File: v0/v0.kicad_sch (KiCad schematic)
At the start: 40 parts, among them CON1 SNES-CONN, U1 SN74LV165APWR, U2 SN74LV165APWR, U3 SN74LV165APWR, U4 SN74LVC8T245PWR, U5 PIC12F629-ISN, U6 AMS1117-3.3, U7 SN74LVC8T245PWR, U8 Pico

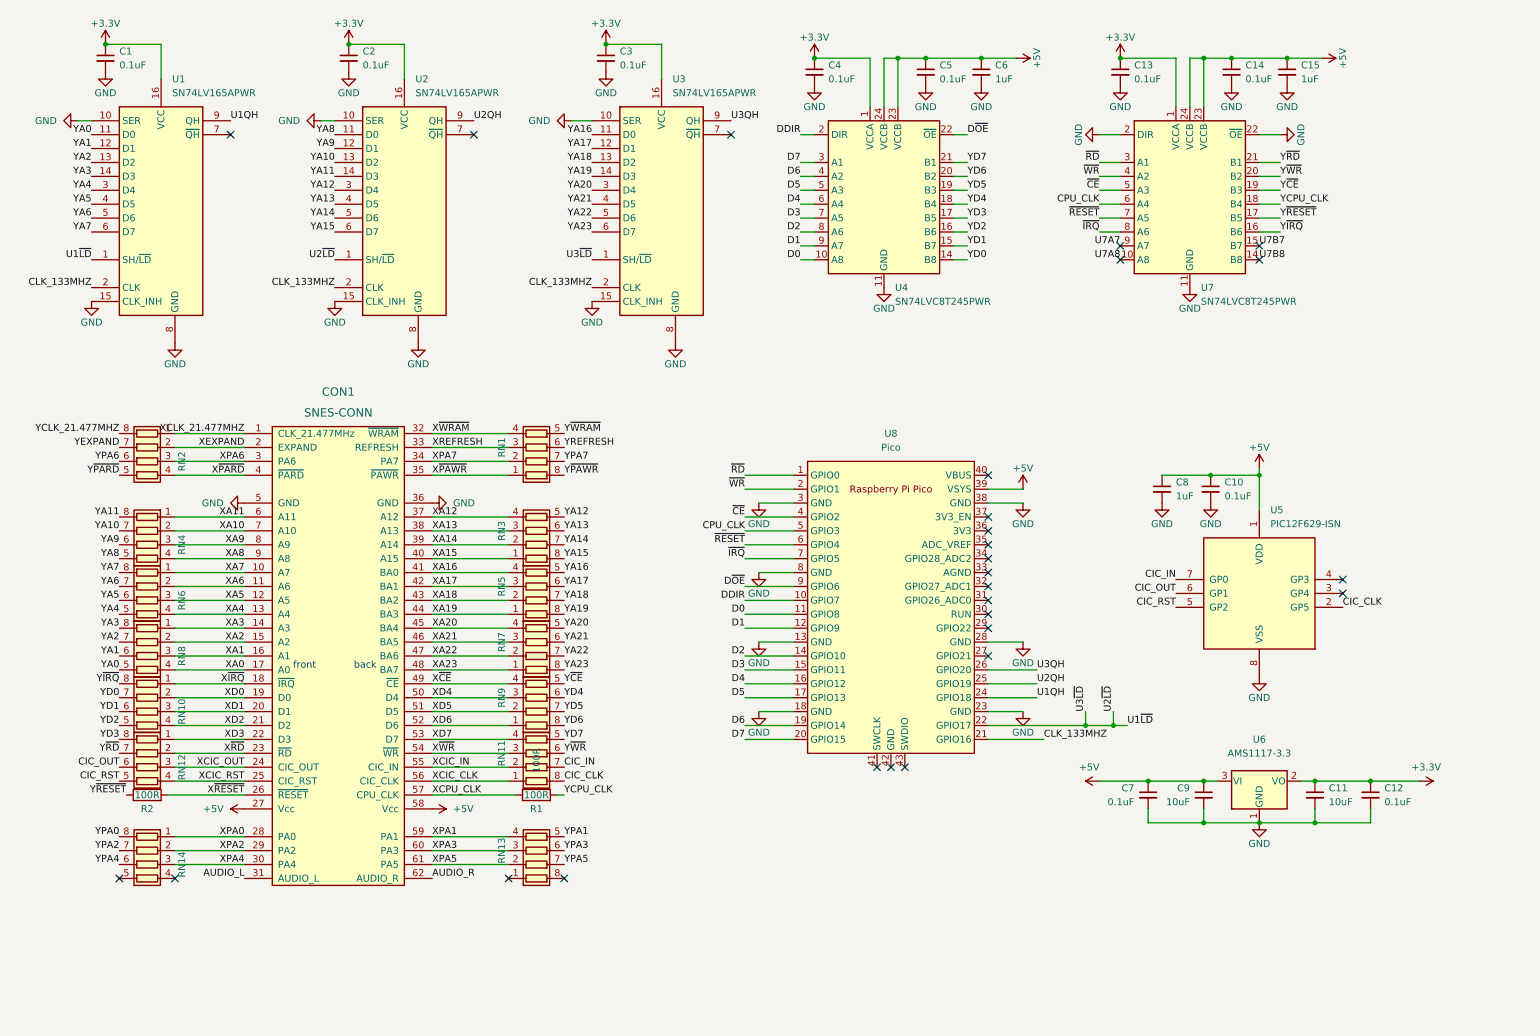
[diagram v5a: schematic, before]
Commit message: Critical fix to PSRAM to control /CE pin from Pico; add LCSC properties to all parts; add ICSP header for PIC12F
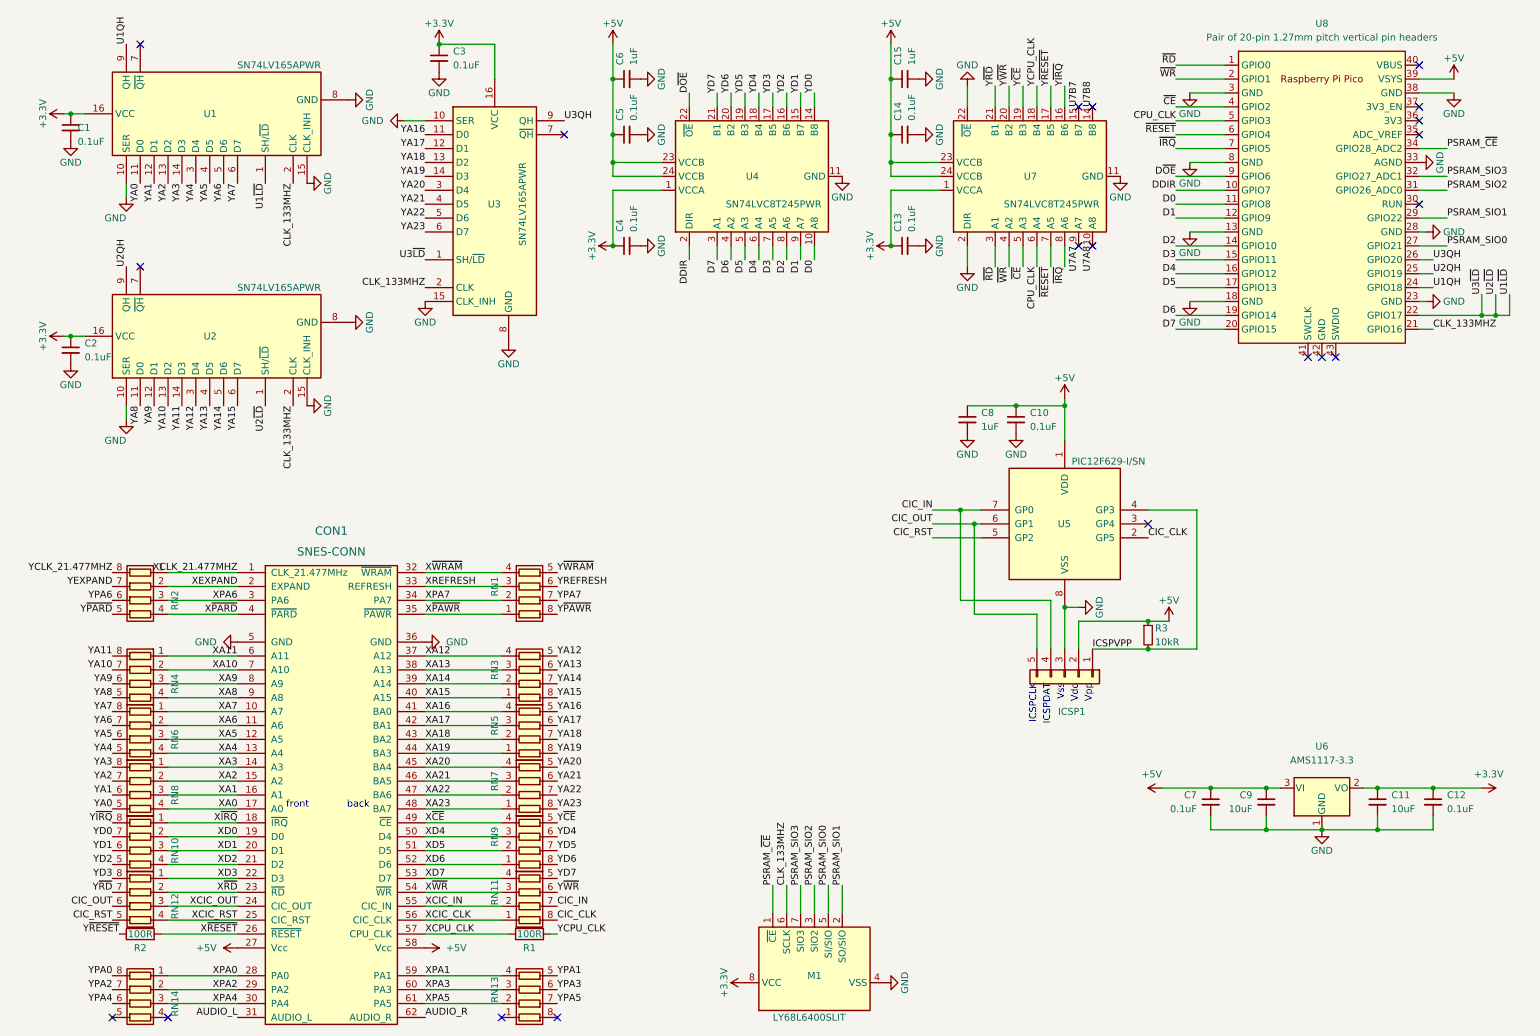
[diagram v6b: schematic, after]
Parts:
- added ICSP1: Conn_01x05, Connector_PinHeader_2.54mm:PinHeader_1x05_P2.54mm_Vertical, symbol Connector_Generic:Conn_01x05
- added M1: LY68L6400SLIT, Package_SO:SOIC-8_3.9x4.9mm_P1.27mm, symbol Memory_RAM:ESP-PSRAM32
- added R3: 10kR, Resistor_SMD:R_1206_3216Metric_Pad1.30x1.75mm_HandSolder, symbol Device:R_Small
- RN1, RN10, RN12, RN13, RN14, RN2, RN3, RN4, RN5, RN6, RN7, RN8: value R_Pack04 -> 100R; LCSC (none) -> C149863
- RN11, RN9: LCSC (none) -> C149863
- U1, U2, U3: LCSC (none) -> C201716
- U4, U7: LCSC (none) -> C27643
- U5: value PIC12F629-ISN -> PIC12F629-I/SN; LCSC (none) -> C8226
- U6: LCSC (none) -> C6186
- U8: value Pico -> Pair of 20-pin 1.27mm pitch vertical pin headers
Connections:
- net +3.3V: now also M1.8 (VCC)
- net +5V: now also ICSP1.2 (Pin_2), R3.1
- net CIC_IN: now also ICSP1.4 (Pin_4)
- net CIC_OUT: now also ICSP1.5 (Pin_5)
- net CLK_133MHZ: now also M1.6 (SCLK)
- net GND: now also U8.33 (AGND), ICSP1.3 (Pin_3), M1.4 (VSS)
- net ICSPVPP: now reaches U5.4 (GP3)
- net ICSPVPP: now also ICSP1.1 (Pin_1), R3.2
- net PSRAM_SIO0: now reaches U8.27 (GPIO21)
- net PSRAM_SIO0: now also M1.5 (SI/SIO)
- net PSRAM_SIO1: now reaches U8.29 (GPIO22)
- net PSRAM_SIO1: now also M1.2 (SO/SIO)
- net PSRAM_SIO2: now reaches U8.31 (GPIO26_ADC0)
- net PSRAM_SIO2: now also M1.3 (SIO2)
- net PSRAM_SIO3: now reaches U8.32 (GPIO27_ADC1)
- net PSRAM_SIO3: now also M1.7 (SIO3)
- net PSRAM_~{CE}: now reaches U8.34 (GPIO28_ADC2)
- net PSRAM_~{CE}: now also M1.1 (~{CE})
- no-connect marks 27 -> 20
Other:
- note added: "ICSPCLK"
- note added: "ICSPDAT"
- note added: "Vdd"
- note added: "Vpp"
- note added: "Vss"
- moved on the sheet: C1, C10, C11, C12, C13, C14, C15, C2, C3, C4, C5, C6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

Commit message: Add JLC properties; re-render front,back,pdf
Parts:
- C1, C10, C11, C12, C13, C14, C15, C2, C3, C4, C5, C6, C7, C8, C9: JLC (none) -> 1206_C
- ICSP1: JLC (none) -> SIP-5_2.5x12.7x2.54P; LCSC (none) -> C492404
- M1: JLC (none) -> SOIC-8
- R1, R2, R3: JLC (none) -> 1206_R
- RN1, RN10, RN11, RN12, RN13, RN14, RN2, RN3, RN4, RN5, RN6, RN7, RN8, RN9: JLC (none) -> RES-ARRAY-SMD
- U1, U2, U3: JLC (none) -> HTSSOP-16_EP_4.4x5.0x0.65P
- U4, U7: JLC (none) -> TSSOP-24_4.4x7.8x0.65P
- U5: JLC (none) -> SOIC-8_3.9x4.9x1.27P
- U6: JLC (none) -> SOT-223
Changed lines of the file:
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@@
+      (effects (font (size 1.27 1.27)) hide)
+    )
+    (property "JLC" "HTSSOP-16_EP_4.4x5.0x0.65P" (id 5) (at 99.06 46.99 0)
       (effects (font (size 1.27 1.27)) hide)
     )
@@
       (effects (font (size 1.27 1.27)) hide)
     )
+    (property "JLC" "HTSSOP-16_EP_4.4x5.0x0.65P" (id 5) (at 46.99 71.12 0)
+      (effects (font (size 1.27 1.27)) hide)
+    )
     (pin "1")
     (pin "10")
@@
     )
     (property "LCSC" "C27643" (id 4) (at 144.78 41.91 90)
+      (effects (font (size 1.27 1.27)) hide)
+    )
+    (property "JLC" "TSSOP-24_4.4x7.8x0.65P" (id 5) (at 144.78 41.91 0)
       (effects (font (size 1.27 1.27)) hide)
     )
@@
       (effects (font (size 1.27 1.27)) hide)
     )
+    (property "JLC" "RES-ARRAY-SMD" (id 5) (at 105.41 172.72 0)
+      (effects (font (size 1.27 1.27)) hide)
+    )
     (pin "1")
     (pin "2")
@@
     )
     (property "LCSC" "C149863" (id 4) (at 105.41 142.24 0)
+      (effects (font (size 1.27 1.27)) hide)
+    )
+    (property "JLC" "RES-ARRAY-SMD" (id 5) (at 105.41 142.24 0)
       (effects (font (size 1.27 1.27)) hide)
     )
@@
       (effects (font (size 1.27 1.27)) hide)
     )
+    (property "JLC" "SOT-223" (id 5) (at 250.19 153.67 0)
+      (effects (font (size 1.27 1.27)) hide)
+    )
     (pin "1")
     (pin "2")
@@
     )
     (property "Datasheet" "~" (id 3) (at 240.03 156.21 0)
+      (effects (font (size 1.27 1.27)) hide)
+    )
+    (property "JLC" "1206_C" (id 4) (at 240.03 156.21 0)
       (effects (font (size 1.27 1.27)) hide)
     )
@@
       (effects (font (size 1.27 1.27)) hide)
     )
+    (property "JLC" "RES-ARRAY-SMD" (id 5) (at 105.41 190.5 0)
+      (effects (font (size 1.27 1.27)) hide)
+    )
     (pin "1")
     (pin "2")
@@
       (effects (font (size 1.27 1.27)) hide)
     )
+    (property "JLC" "RES-ARRAY-SMD" (id 5) (at 34.29 144.78 0)
+      (effects (font (size 1.27 1.27)) hide)
+    )
     (pin "1")
     (pin "2")
@@
     )
     (property "Datasheet" "~" (id 3) (at 123.19 34.29 0)
+      (effects (font (size 1.27 1.27)) hide)
+    )
+    (property "JLC" "1206_C" (id 4) (at 123.19 34.29 0)
       (effects (font (size 1.27 1.27)) hide)
     )
@@
       (effects (font (size 1.27 1.27)) hide)
     )
+    (property "JLC" "1206_R" (id 4) (at 105.41 180.34 0)
+      (effects (font (size 1.27 1.27)) hide)
+    )
     (pin "1")
     (pin "2")
@@
     )
     (property "Datasheet" "~" (id 3) (at 270.51 156.21 0)
+      (effects (font (size 1.27 1.27)) hide)
+    )
+    (property "JLC" "1206_C" (id 4) (at 270.51 156.21 0)
       (effects (font (size 1.27 1.27)) hide)
     )
@@
       (effects (font (size 1.27 1.27)) hide)
     )
+    (property "JLC" "RES-ARRAY-SMD" (id 5) (at 34.29 154.94 0)
+      (effects (font (size 1.27 1.27)) hide)
+    )
     (pin "1")
     (pin "2")
@@
     )
     (property "LCSC" "C27643" (id 4) (at 195.58 41.91 90)
+      (effects (font (size 1.27 1.27)) hide)
+    )
+    (property "JLC" "TSSOP-24_4.4x7.8x0.65P" (id 5) (at 195.58 41.91 0)
       (effects (font (size 1.27 1.27)) hide)
     )
@@
       (effects (font (size 1.27 1.27)) hide)
     )
+    (property "JLC" "RES-ARRAY-SMD" (id 5) (at 34.29 119.38 0)
+      (effects (font (size 1.27 1.27)) hide)
+    )
     (pin "1")
     (pin "2")
@@
     )
     (property "Datasheet" "~" (id 3) (at 260.35 156.21 0)
+      (effects (font (size 1.27 1.27)) hide)
+    )
+    (property "JLC" "1206_C" (id 4) (at 260.35 156.21 0)
       (effects (font (size 1.27 1.27)) hide)
     )
@@
       (effects (font (size 1.27 1.27)) hide)
     )
+    (property "JLC" "RES-ARRAY-SMD" (id 5) (at 34.29 175.26 0)
+      (effects (font (size 1.27 1.27)) hide)
+    )
     (pin "1")
     (pin "2")
@@
       (effects (font (size 1.27 1.27)) hide)
     )
+    (property "JLC" "RES-ARRAY-SMD" (id 5) (at 34.29 134.62 0)
+      (effects (font (size 1.27 1.27)) hide)
+    )
     (pin "1")
     (pin "2")
@@
     )
     (property "LCSC" "C201716" (id 4) (at 46.99 30.48 0)
+      (effects (font (size 1.27 1.27)) hide)
+    )
+    (property "JLC" "HTSSOP-16_EP_4.4x5.0x0.65P" (id 5) (at 46.99 30.48 0)
       (effects (font (size 1.27 1.27)) hide)
     )
@@
       (effects (font (size 1.27 1.27)) hide)
     )
+    (property "JLC" "1206_C" (id 4) (at 185.42 86.36 0)
+      (effects (font (size 1.27 1.27)) hide)
+    )
     (pin "1")
     (pin "2")
@@
       (effects (font (size 1.27 1.27)) hide)
     )
+    (property "JLC" "1206_C" (id 4) (at 194.31 86.36 0)
+      (effects (font (size 1.27 1.27)) hide)
+    )
     (pin "1")
     (pin "2")
@@
       (effects (font (size 1.27 1.27)) hide)
     )
+    (property "JLC" "1206_C" (id 4) (at 21.59 73.66 0)
+      (effects (font (size 1.27 1.27)) hide)
+    )
     (pin "1")
     (pin "2")
@@
       (effects (font (size 1.27 1.27)) hide)
     )
+    (property "JLC" "RES-ARRAY-SMD" (id 5) (at 34.29 193.04 0)
+      (effects (font (size 1.27 1.27)) hide)
+    )
     (pin "1")
     (pin "2")
@@
       (effects (font (size 1.27 1.27)) hide)
     )
+    (property "JLC" "1206_C" (id 4) (at 88.9 20.32 0)
+      (effects (font (size 1.27 1.27)) hide)
+    )
     (pin "1")
     (pin "2")
@@
     )
     (property "Datasheet" "~" (id 3) (at 123.19 54.61 0)
+      (effects (font (size 1.27 1.27)) hide)
+    )
+    (property "JLC" "1206_C" (id 4) (at 123.19 54.61 0)
       (effects (font (size 1.27 1.27)) hide)
     )
@@
       (effects (font (size 1.27 1.27)) hide)
     )
+    (property "JLC" "RES-ARRAY-SMD" (id 5) (at 105.41 152.4 0)
+      (effects (font (size 1.27 1.27)) hide)
+    )
     (pin "1")
     (pin "2")
@@
     )
     (property "Datasheet" "~" (id 3) (at 229.87 156.21 0)
+      (effects (font (size 1.27 1.27)) hide)
+    )
+    (property "JLC" "1206_C" (id 4) (at 229.87 156.21 0)
       (effects (font (size 1.27 1.27)) hide)
     )
@@
       (effects (font (size 1.27 1.27)) hide)
     )
+    (property "JLC" "SOIC-8_3.9x4.9x1.27P" (id 5) (at 203.2 105.41 0)
+      (effects (font (size 1.27 1.27)) hide)
+    )
     (pin "1")
     (pin "2")
@@
       (effects (font (size 1.27 1.27)) hide)
     )
+    (property "JLC" "RES-ARRAY-SMD" (id 5) (at 105.41 132.08 0)
+      (effects (font (size 1.27 1.27)) hide)
+    )
     (pin "1")
     (pin "2")
@@
     )
     (property "Datasheet" "~" (id 3) (at 173.99 54.61 0)
+      (effects (font (size 1.27 1.27)) hide)
+    )
+    (property "JLC" "1206_C" (id 4) (at 173.99 54.61 0)
       (effects (font (size 1.27 1.27)) hide)
     )
@@
       (effects (font (size 1.27 1.27)) hide)
     )
+    (property "JLC" "SOIC-8" (id 5) (at 157.48 186.69 0)
+      (effects (font (size 1.27 1.27)) hide)
+    )
     (pin "1")
     (pin "2")
@@
     )
     (property "Datasheet" "~" (id 3) (at 21.59 33.02 0)
+      (effects (font (size 1.27 1.27)) hide)
+    )
+    (property "JLC" "1206_C" (id 4) (at 21.59 33.02 0)
       (effects (font (size 1.27 1.27)) hide)
     )
@@
       (effects (font (size 1.27 1.27)) hide)
     )
+    (property "LCSC" "C492404" (id 4) (at 203.2 133.35 90)
+      (effects (font (size 1.27 1.27)) hide)
+    )
+    (property "JLC" "SIP-5_2.5x12.7x2.54P" (id 5) (at 203.2 133.35 90)
+      (effects (font (size 1.27 1.27)) hide)
+    )
     (pin "1")
     (pin "2")
@@
     )
     (property "LCSC" "C149863" (id 4) (at 34.29 165.1 0)
+      (effects (font (size 1.27 1.27)) hide)
+    )
+    (property "JLC" "RES-ARRAY-SMD" (id 5) (at 34.29 165.1 0)
       (effects (font (size 1.27 1.27)) hide)
     )
@@
       (effects (font (size 1.27 1.27)) hide)
     )
+    (property "JLC" "1206_R" (id 4) (at 34.29 180.34 0)
+      (effects (font (size 1.27 1.27)) hide)
+    )
     (pin "1")
     (pin "2")
@@
       (effects (font (size 1.27 1.27)) hide)
     )
+    (property "JLC" "1206_R" (id 4) (at 218.44 125.73 0)
+      (effects (font (size 1.27 1.27)) hide)
+    )
     (pin "1")
     (pin "2")
@@
       (effects (font (size 1.27 1.27)) hide)
     )
+    (property "JLC" "1206_C" (id 4) (at 173.99 24.13 0)
+      (effects (font (size 1.27 1.27)) hide)
+    )
     (pin "1")
     (pin "2")
@@
     )
     (property "Datasheet" "~" (id 3) (at 173.99 34.29 0)
+      (effects (font (size 1.27 1.27)) hide)
+    )
+    (property "JLC" "1206_C" (id 4) (at 173.99 34.29 0)
       (effects (font (size 1.27 1.27)) hide)
     )
@@
       (effects (font (size 1.27 1.27)) hide)
     )
+    (property "JLC" "1206_C" (id 4) (at 123.19 24.13 0)
+      (effects (font (size 1.27 1.27)) hide)
+    )
     (pin "1")
     (pin "2")
@@
       (effects (font (size 1.27 1.27)) hide)
     )
+    (property "JLC" "RES-ARRAY-SMD" (id 5) (at 105.41 116.84 0)
+      (effects (font (size 1.27 1.27)) hide)
+    )
     (pin "1")
     (pin "2")
@@
       (effects (font (size 1.27 1.27)) hide)
     )
+    (property "JLC" "RES-ARRAY-SMD" (id 5) (at 105.41 162.56 0)
+      (effects (font (size 1.27 1.27)) hide)
+    )
